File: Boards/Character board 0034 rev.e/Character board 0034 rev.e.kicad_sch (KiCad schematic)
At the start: 40 parts, among them J1 card edge, J2 character connector, J3 power jumper, J4 return jumper, Q1 TIP130A, U1 2.2K, U1 6821, U2 2.2K, U4 ULN2003A, U5 7406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

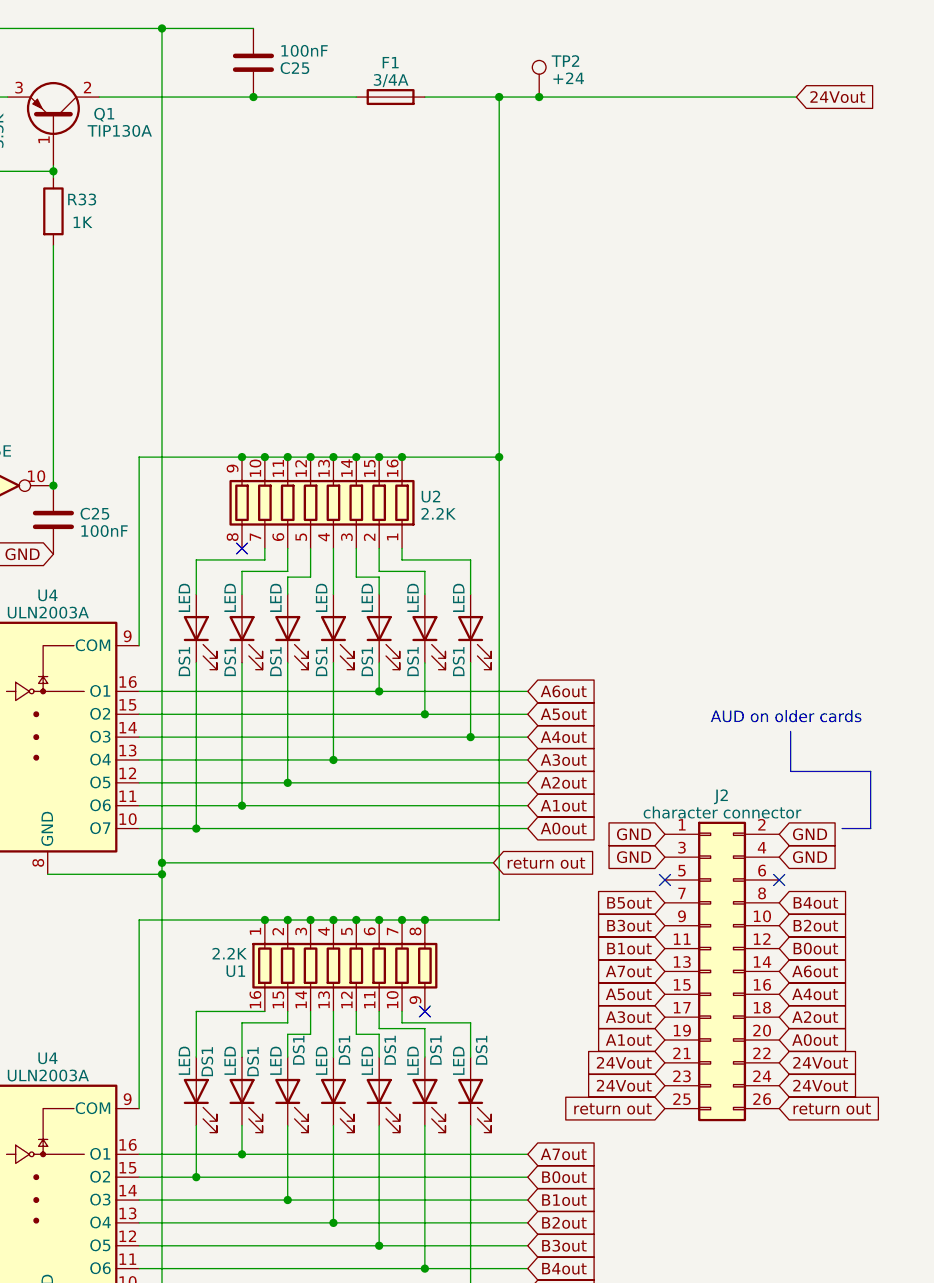
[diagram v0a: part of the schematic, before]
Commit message: finish light board rev.a, rename files, add renders and schematics, move pictures
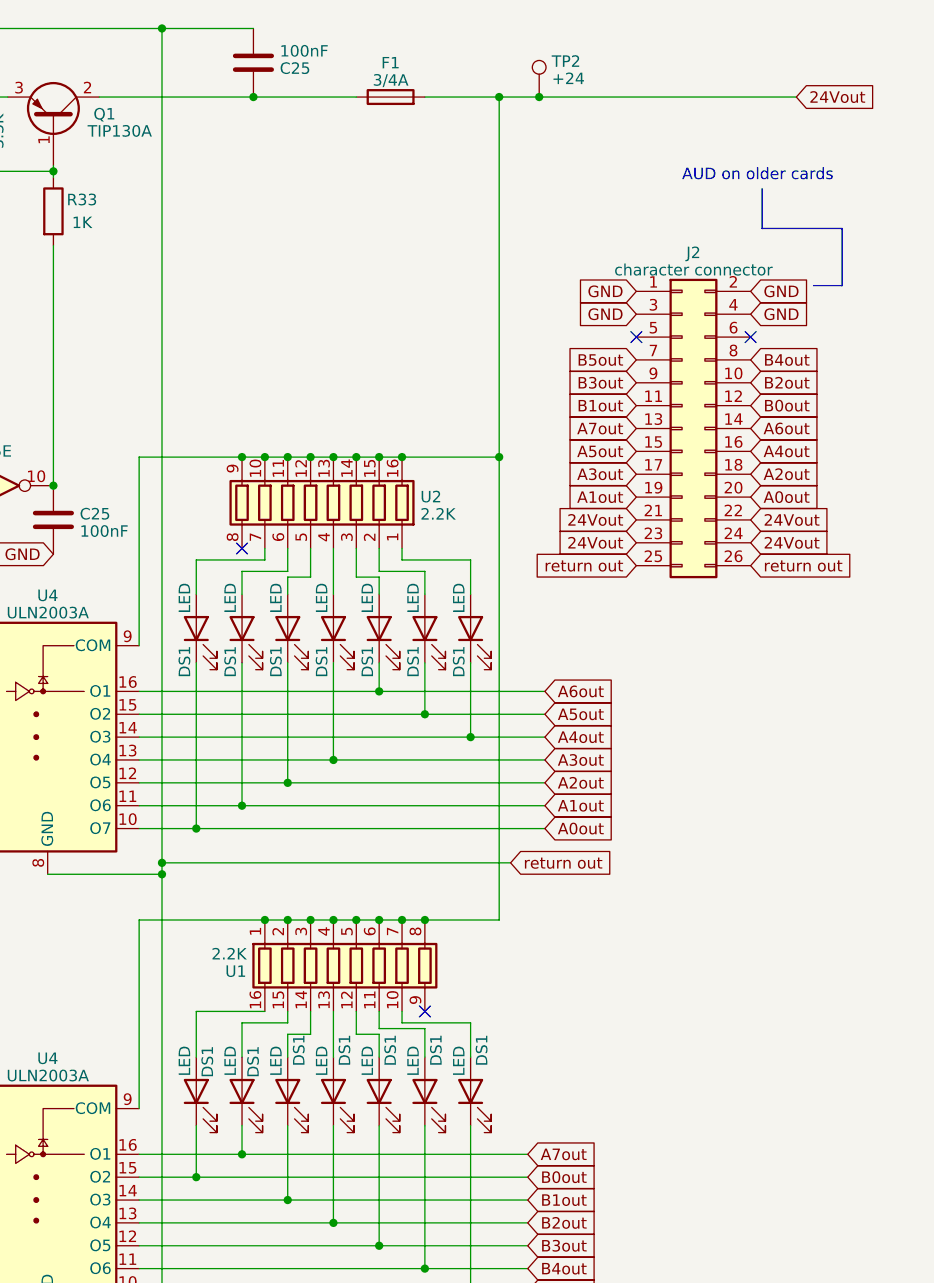
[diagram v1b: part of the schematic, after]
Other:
- moved on the sheet: J2

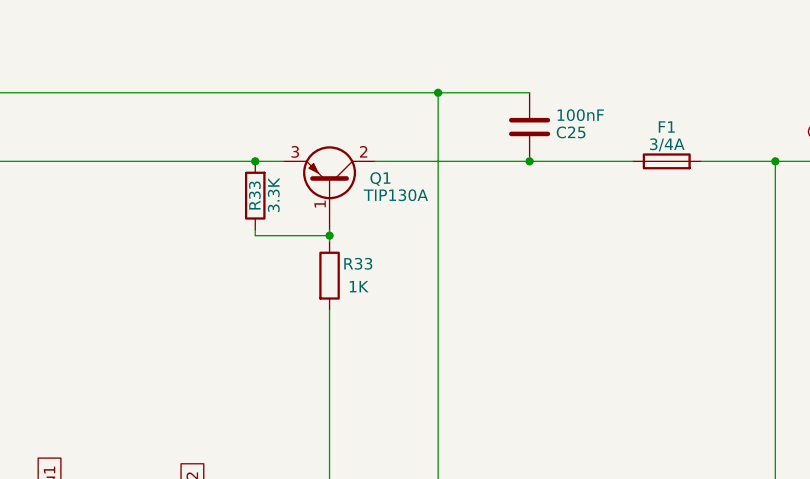
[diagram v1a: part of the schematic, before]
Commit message: revisions from real life boards
tip130a is actually tip30a, widened holes for crystal, widened holes for big power resistor, fixed cpu board LED resistors
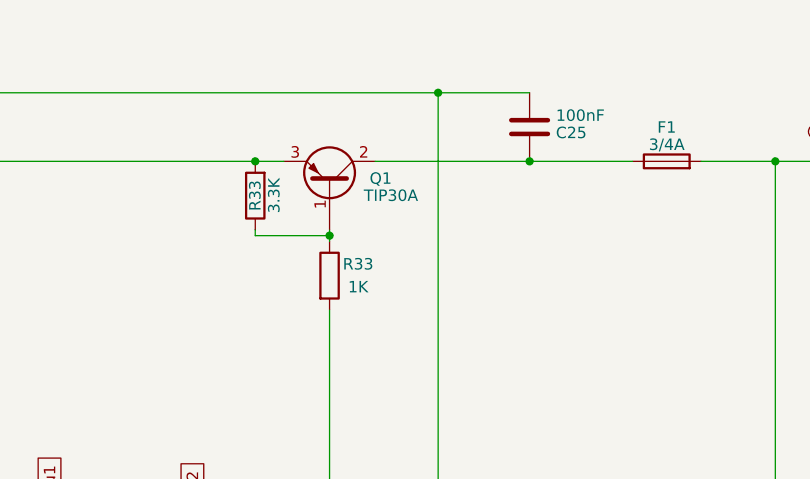
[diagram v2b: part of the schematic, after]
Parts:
- Q1: value TIP130A -> TIP30A
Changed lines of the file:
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@@
       (effects (font (size 1.27 1.27)) (justify left))
     )
-    (property "Value" "TIP130A" (at 177.8 31.75 90)
+    (property "Value" "TIP30A" (at 177.8 31.75 90)
       (effects (font (size 1.27 1.27)) (justify left))
     )
